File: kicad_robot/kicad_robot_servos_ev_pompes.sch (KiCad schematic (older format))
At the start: 60 parts

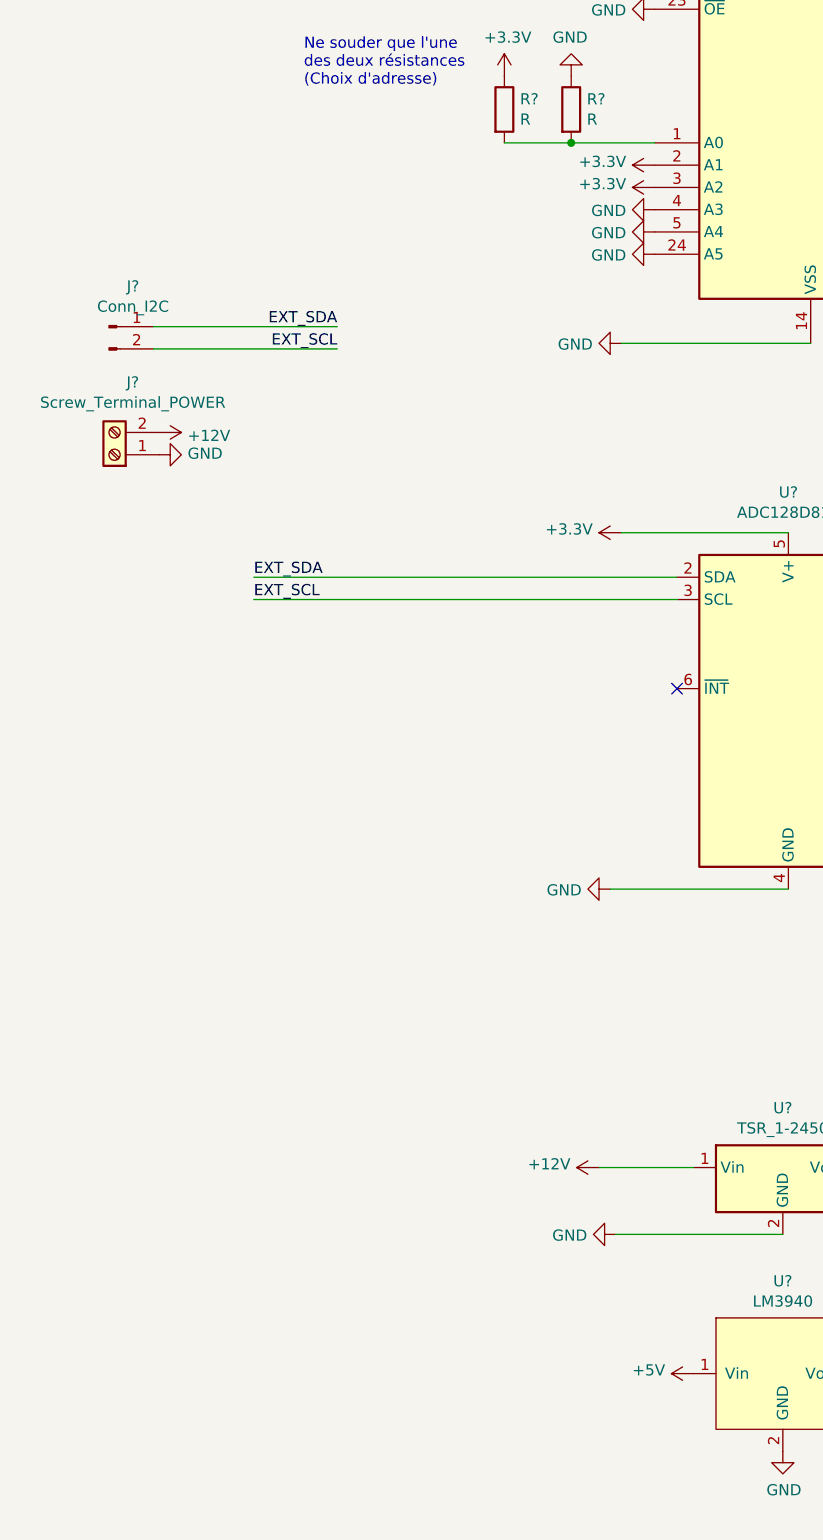
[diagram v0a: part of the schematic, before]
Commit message: Séparation de l'alimentation du LM3940
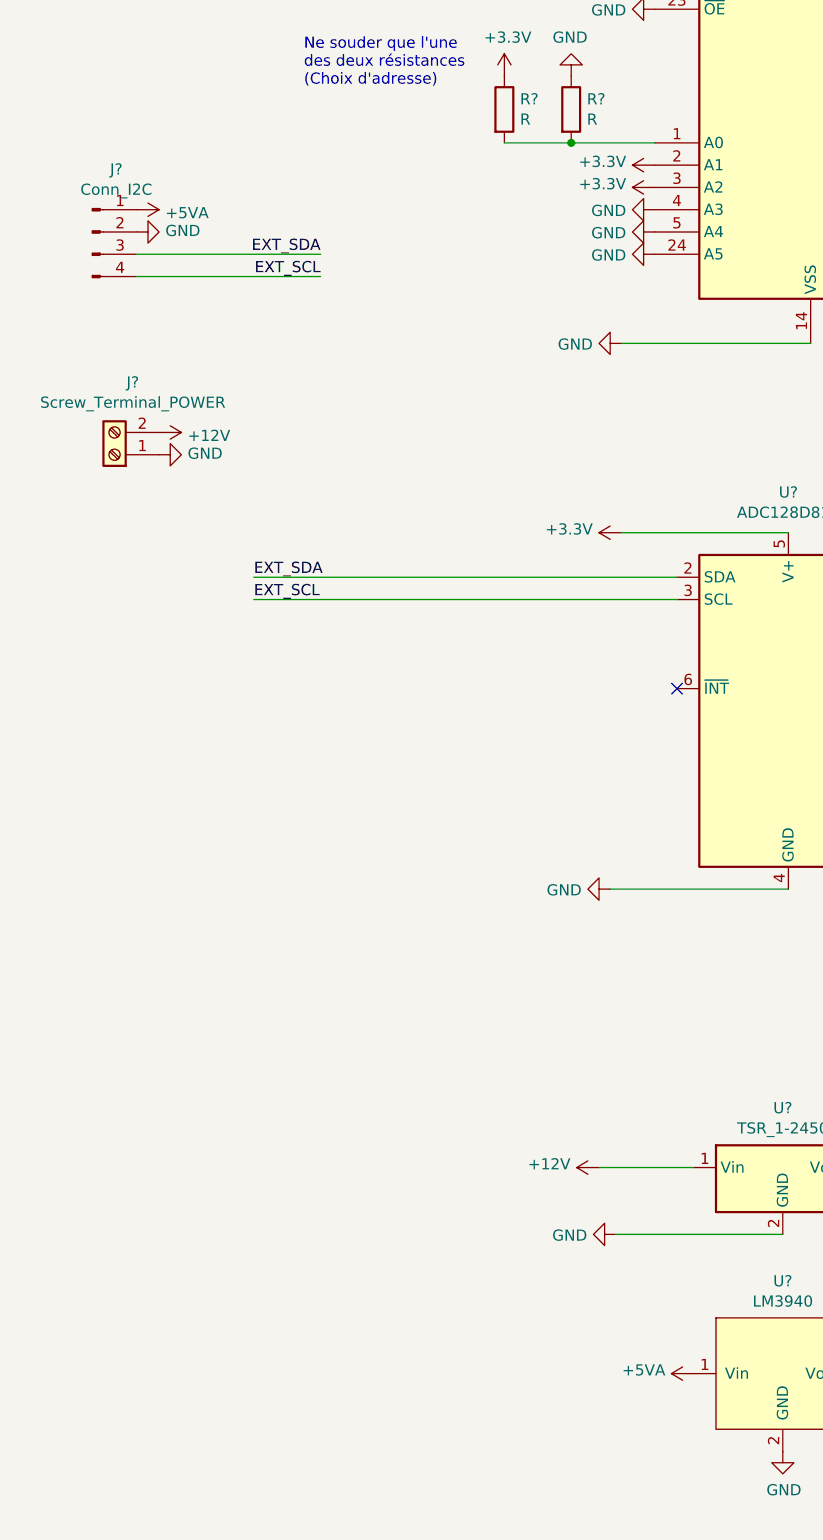
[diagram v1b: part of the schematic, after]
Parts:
- removed J?: Conn_I2C, symbol Connector:Conn_01x02_Male
- added J?: Conn_I2C, symbol Connector:Conn_01x04_Male
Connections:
- net +5V: no longer U?.1 (Vin)
- net EXT_SCL: now also J?.4 (Pin_4)
- net EXT_SDA: now also J?.3 (Pin_3)
- net GND: now also J?.2 (Pin_2)
- new net +5VA: J?.1 (Pin_1), U?.1 (Vin)
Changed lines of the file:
@@
 	-1   0    0    1
 $EndComp
-$Comp
-L Connector:Conn_01x02_Male J?
-U 1 1 604FCCE9
-P 800 3875
-F 0 "J?" H 908 4056 50  0000 C CNN
-F 1 "Conn_I2C" H 908 3965 50  0000 C CNN
-F 2 "" H 800 3875 50  0001 C CNN
-F 3 "~" H 800 3875 50  0001 C CNN
-	1    800  3875
-	1    0    0    -1
-$EndComp
 Wire Wire Line
-	1000 3875 1825 3875
+	925  3550 1750 3550
 Wire Wire Line
-	1000 3975 1825 3975
-Text Label 1825 3875 2    50   ~ 0
+	925  3650 1750 3650
+Text Label 1750 3550 2    50   ~ 0
 EXT_SDA
-Text Label 1825 3975 2    50   ~ 0
+Text Label 1750 3650 2    50   ~ 0
 EXT_SCL
 $Comp
@@
 $EndComp
 $Comp
-L power:+5V #PWR?
-U 1 1 6034D6D8
-P 3425 8575
-F 0 "#PWR?" H 3425 8425 50  0001 C CNN
-F 1 "+5V" V 3440 8703 50  0000 L CNN
-F 2 "" H 3425 8575 50  0001 C CNN
-F 3 "" H 3425 8575 50  0001 C CNN
-	1    3425 8575
-	0    -1   -1   0
-$EndComp
-$Comp
 L power:+3.3V #PWR?
 U 1 1 6034EA05
@@
 Text Notes 5225 5975 0    50   ~ 0
 Ne souder que l'une\ndes deux résistances\n(Choix d'adresse)
+$Comp
+L Connector:Conn_01x04_Male J?
+U 1 1 603BA60C
+P 725 3450
+F 0 "J?" H 833 3731 50  0000 C CNN
+F 1 "Conn_I2C" H 833 3640 50  0000 C CNN
+F 2 "" H 725 3450 50  0001 C CNN
+F 3 "~" H 725 3450 50  0001 C CNN
+	1    725  3450
+	1    0    0    -1
+$EndComp
+$Comp
+L power:GND #PWR?
+U 1 1 603D1DF0
+P 925 3450
+F 0 "#PWR?" H 925 3200 50  0001 C CNN
+F 1 "GND" V 930 3322 50  0000 R CNN
+F 2 "" H 925 3450 50  0001 C CNN
+F 3 "" H 925 3450 50  0001 C CNN
+	1    925  3450
+	0    -1   -1   0
+$EndComp
+$Comp
+L power:+5VA #PWR?
+U 1 1 603D403F
+P 925 3350
+F 0 "#PWR?" H 925 3200 50  0001 C CNN
+F 1 "+5VA" V 940 3478 50  0000 L CNN
+F 2 "" H 925 3350 50  0001 C CNN
+F 3 "" H 925 3350 50  0001 C CNN
+	1    925  3350
+	0    1    1    0
+$EndComp
+$Comp
+L power:+5VA #PWR?
+U 1 1 603E1908
+P 3425 8575
+F 0 "#PWR?" H 3425 8425 50  0001 C CNN
+F 1 "+5VA" V 3440 8702 50  0000 L CNN
+F 2 "" H 3425 8575 50  0001 C CNN
+F 3 "" H 3425 8575 50  0001 C CNN
+	1    3425 8575
+	0    -1   -1   0
+$EndComp
 $EndSCHEMATC
